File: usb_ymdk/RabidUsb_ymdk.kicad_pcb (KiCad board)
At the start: 2 copper layers, 40.6 x 16.8 mm, 16 parts, among them J1 USB_C_Receptacle_USB2.0, J2 Conn_01x04, U1 SRV05-4

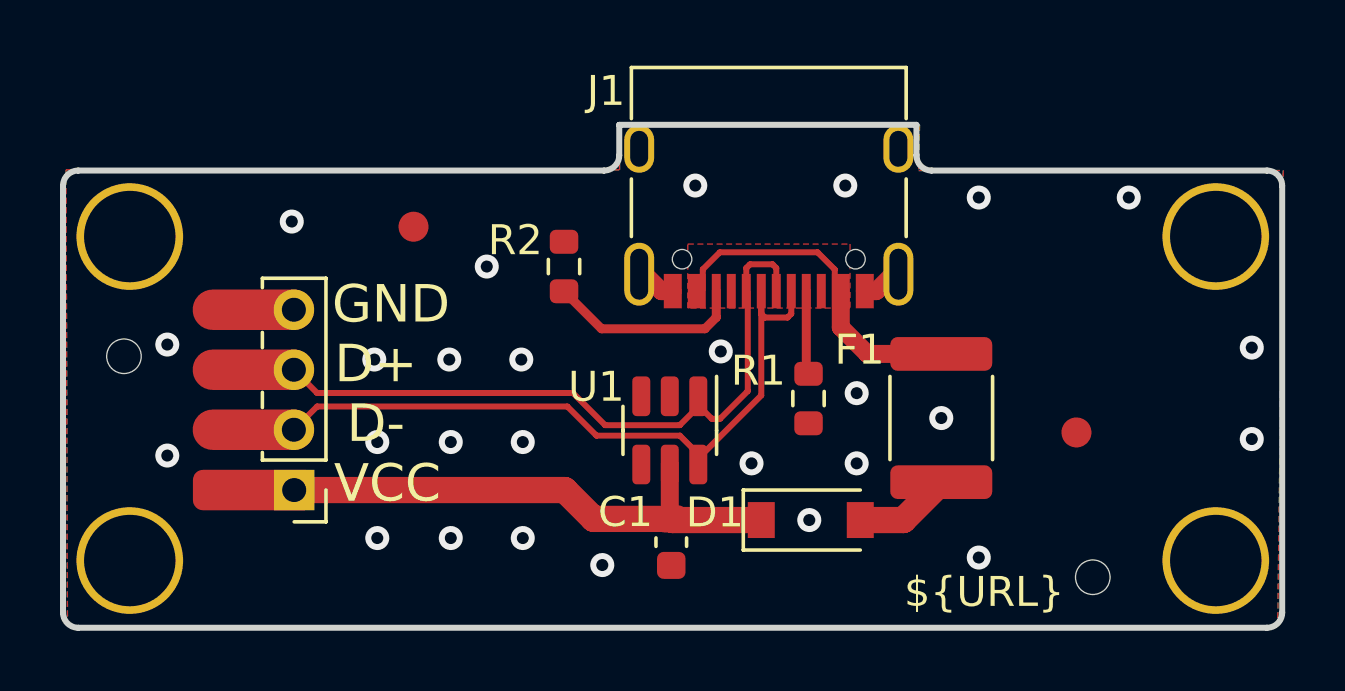
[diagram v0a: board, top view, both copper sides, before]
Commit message: USB: More ground plane between VCC and D+/D-.
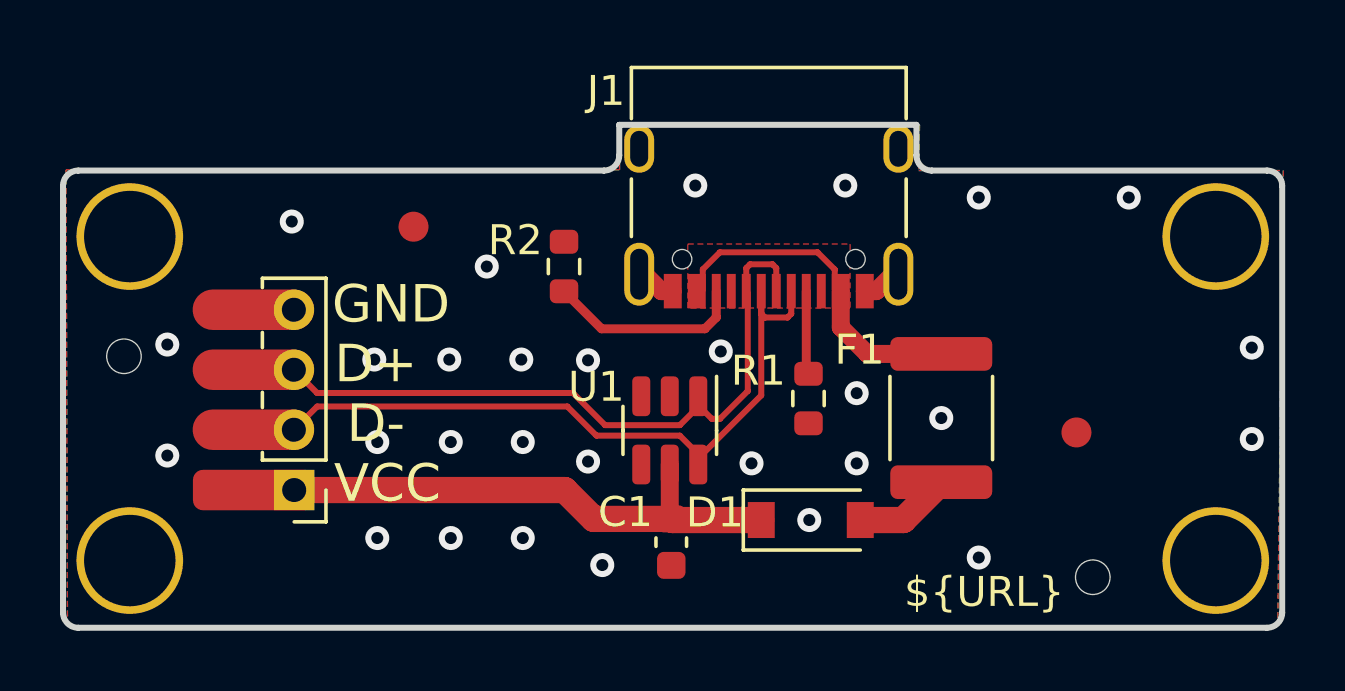
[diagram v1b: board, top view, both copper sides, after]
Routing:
- net GND: vias 27 -> 29
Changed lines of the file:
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@@
   (via (at 131.4 59.53) (size 0.8) (drill 0.4) (layers "F.Cu" "B.Cu") (free) (net 2))
   (via (at 124.8 65.75) (size 0.8) (drill 0.4) (layers "F.Cu" "B.Cu") (free) (net 2))
+  (via (at 126.975 59.825) (size 0.8) (drill 0.4) (layers "F.Cu" "B.Cu") (free) (net 2))
   (via (at 112.95 59.3) (size 0.8) (drill 0.4) (layers "F.Cu" "B.Cu") (free) (net 2))
   (via (at 117.1 55.2) (size 0.8) (drill 0.4) (layers "F.Cu" "B.Cu") (free) (net 2))
@@
   (via (at 122.4 65.75) (size 0.8) (drill 0.4) (layers "F.Cu" "B.Cu") (free) (net 2))
   (via (at 112.95 63) (size 0.8) (drill 0.4) (layers "F.Cu" "B.Cu") (free) (net 2))
+  (via (at 126.975 63.2) (size 0.8) (drill 0.4) (layers "F.Cu" "B.Cu") (free) (net 2))
   (via (at 122.4 62.55) (size 0.8) (drill 0.4) (layers "F.Cu" "B.Cu") (free) (net 2))
   (via (at 149.1 59.402) (size 0.8) (drill 0.4) (layers "F.Cu" "B.Cu") (free) (net 2))

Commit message: USB: Add ferrite beads to YMDK USB board.
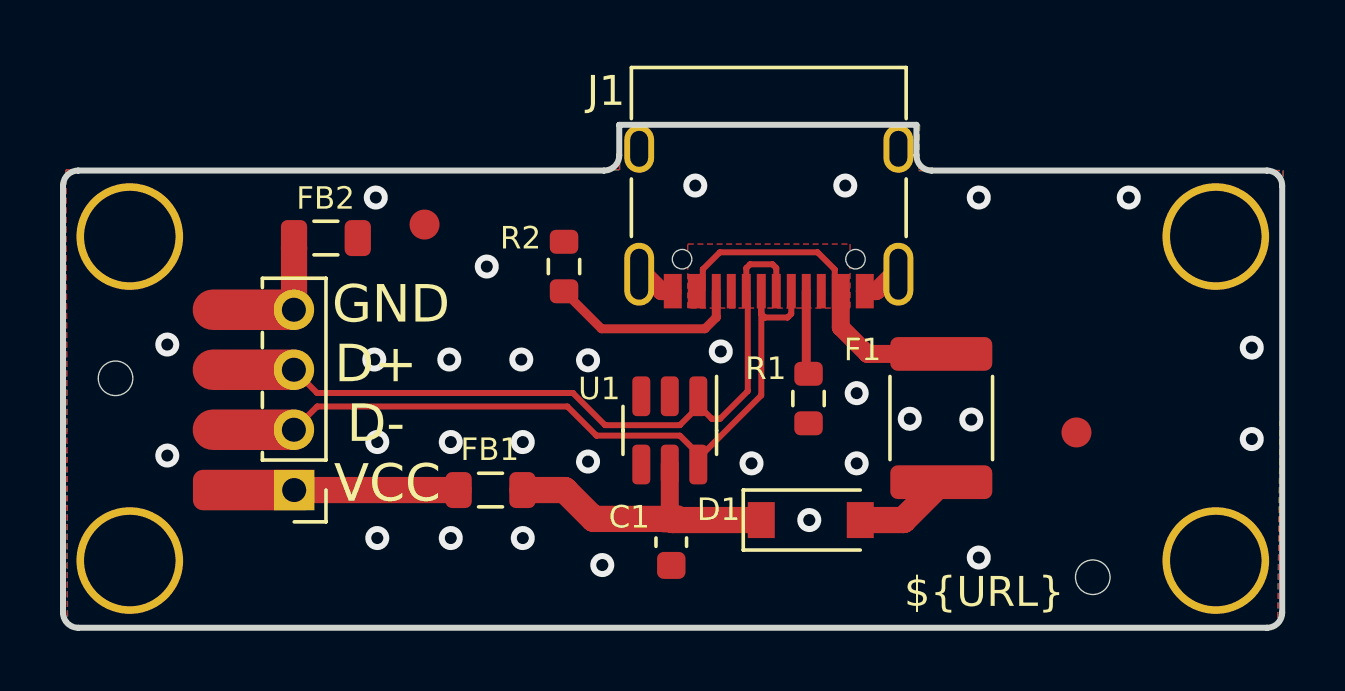
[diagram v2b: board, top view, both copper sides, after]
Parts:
- added FB1: FerriteBead_Small, Inductor_SMD:L_0805_2012Metric, F.Cu at (123.7, 64.2)
- added FB2: FerriteBead_Small, Inductor_SMD:L_0805_2012Metric, F.Cu at (118.2, 55.8)
- moved H8 0.79 mm to (111.2, 60.4)
- moved FID1 0.37 mm to (121.5, 55.3)
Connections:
- J2 pad 1: VCC -> Net-(FB1-Pad2)
- J2 pad 4: GND -> Net-(FB2-Pad1)
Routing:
- net VCC: track 17.8 -> 10.2 mm
- net Net-(FB1-Pad2): track 0.00 -> 5.48 mm
- net Net-(FB2-Pad1): track 0.00 -> 2.09 mm
- net GND: vias 29 -> 30
